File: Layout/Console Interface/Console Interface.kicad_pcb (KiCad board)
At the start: 2 copper layers, 25.5 x 5 mm, 54 parts, among them J1 USB_C_Receptacle_USB2.0, J2 Conn_01x04_Socket, J3 Conn_01x04_Socket, J4 Conn_01x04_Socket, J6 Conn_01x04_Socket, Q1 AO3401A, SW1 SW_BOOT, U1 W25Q32JVSS, U2 RP2040, U5 MIC5504-3.3YM5, Y1 Crystal_GND24

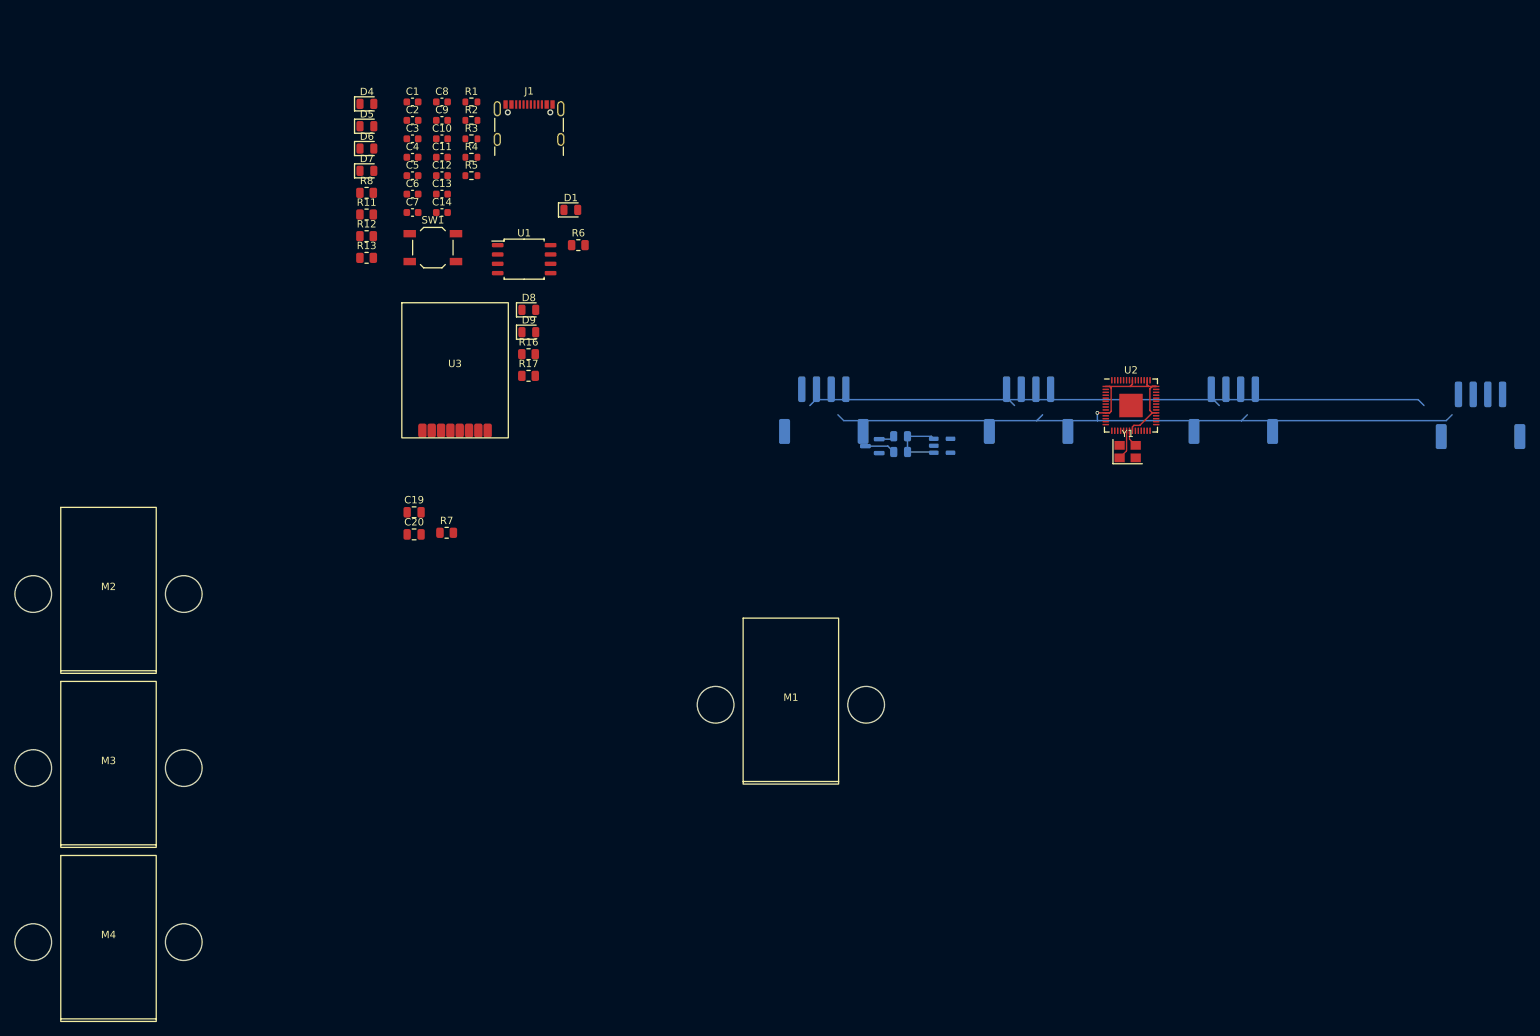
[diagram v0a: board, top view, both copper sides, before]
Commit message: Add console interface schematic
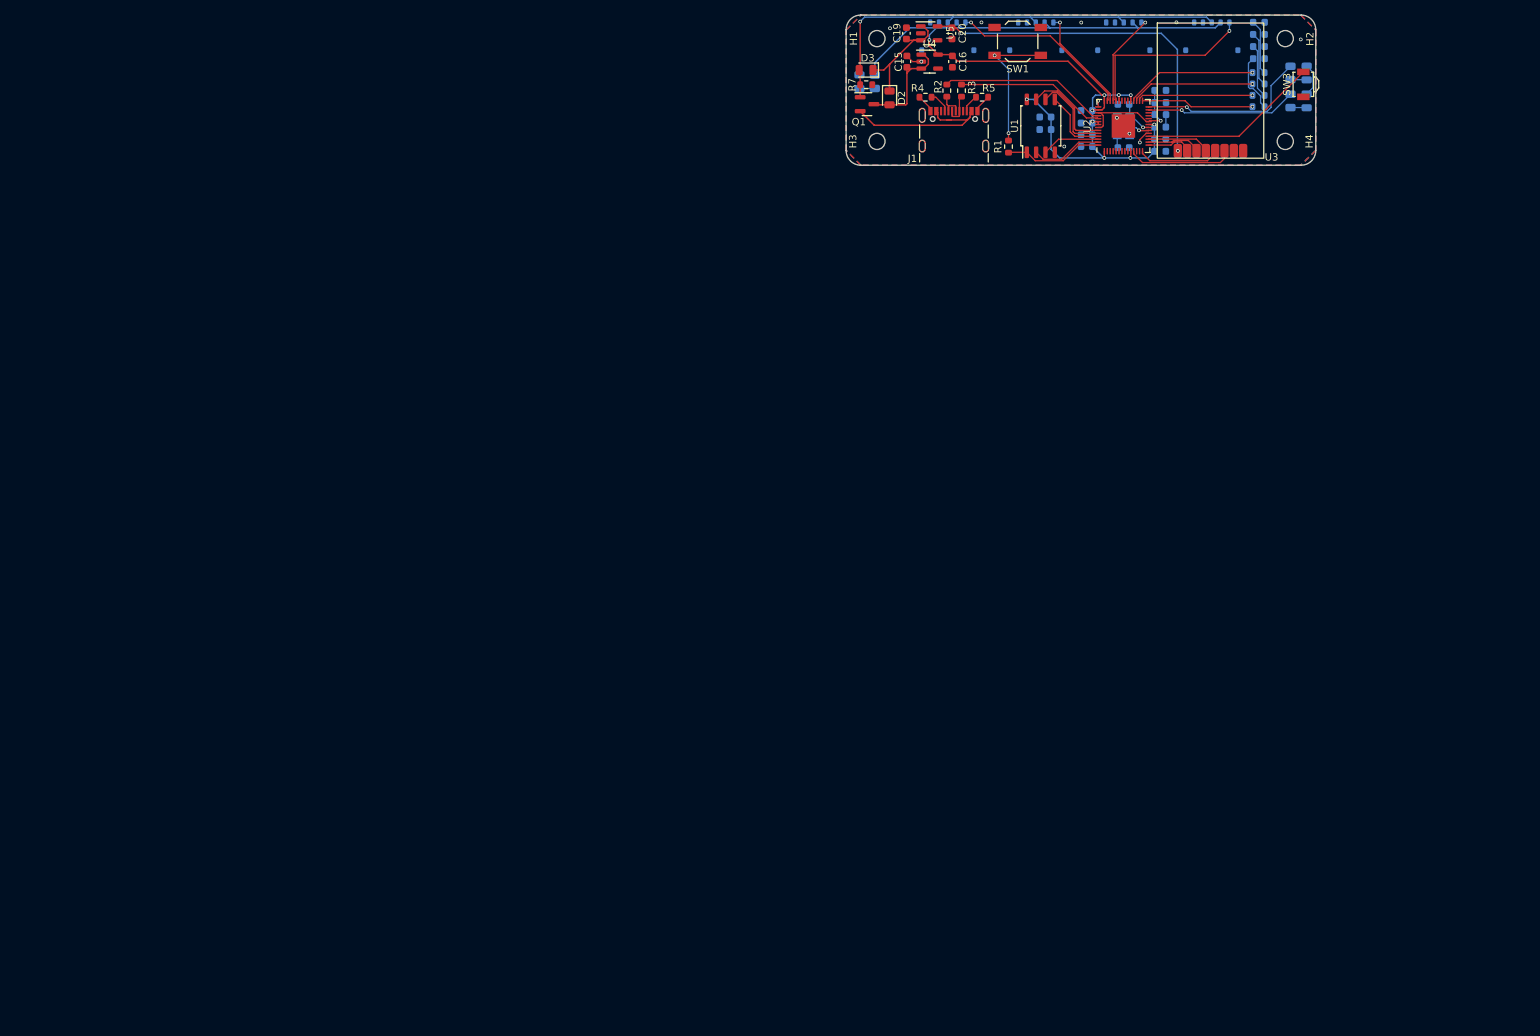
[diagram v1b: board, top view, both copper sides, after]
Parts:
- removed M1, M2, M3, M4: ~, GameCube Controllers:Controller Plug Clamp
- added C15: C, Capacitor_SMD:C_0603_1608Metric, F.Cu at (162.4, 39.6)
- added C16: C, Capacitor_SMD:C_0603_1608Metric, F.Cu at (168.6, 39.6)
- added H1: MountingHole, MountingHole:MountingHole_2.2mm_M2, F.Cu at (158.4, 36.5)
- added H2: MountingHole, MountingHole:MountingHole_2.2mm_M2, F.Cu at (214.0, 36.5)
- added H3: MountingHole, MountingHole:MountingHole_2.2mm_M2, F.Cu at (158.4, 50.5)
- added H4: MountingHole, MountingHole:MountingHole_2.2mm_M2, F.Cu at (214.0, 50.5)
- added SW3: SW_PAIR, Button_Switch_SMD:SW_SPST_B3U-3000P, F.Cu at (216.4, 42.7)
- added U4: MIC5504-3.3YM5, Package_TO_SOT_SMD:SOT-23-5, F.Cu at (165.5, 39.6)
- C1, C10, C11, C12, C13, C14, C2, C3, C4, C5, C6, C7, C8, C9, D1, D8, D9, R16, R17, R6, Y1: moved to B.Cu
- C19, C20: footprint Capacitor_SMD:C_0805_2012Metric -> Capacitor_SMD:C_0603_1608Metric
- D2, D3, Q1, U5: moved to F.Cu
- D4, D5, D6, D7: footprint LED_SMD:LED_0805_2012Metric -> LED_SMD:LED_0603_1608Metric; moved to B.Cu
- J2, J3, J4, J6: footprint Connector_JST:JST_PH_S4B-PH-SM4-TB_1x04-1MP_P2.00mm_Horizontal -> Connector_Molex:Molex_Pico-EZmate_78171-0005_1x05-1MP_P1.20mm_Vertical
- R11, R12, R13, R8: footprint Resistor_SMD:R_0805_2012Metric -> Resistor_SMD:R_0603_1608Metric; moved to B.Cu
- R7: footprint Resistor_SMD:R_0805_2012Metric -> Resistor_SMD:R_0603_1608Metric
- moved R13 123.2 mm to (210.3, 45.7)
- moved R12 123.0 mm to (210.3, 44.2)
- moved R11 122.8 mm to (210.3, 42.6)
- moved R8 122.6 mm to (210.3, 41.1)
- moved D7 122.4 mm to (210.4, 39.2), turned to 180 degrees
- moved D6 122.3 mm to (210.4, 37.5), turned to 180 degrees
- moved D5 122.1 mm to (210.4, 35.9), turned to 180 degrees
- moved D4 122.0 mm to (210.4, 34.2), turned to 180 degrees
- moved D8 110.7 mm to (216.9, 41.1), turned to -90 degrees
- moved R16 110.6 mm to (214.7, 41.1), turned to -90 degrees
- moved D9 110.5 mm to (216.9, 44.9), turned to -90 degrees
- moved R17 110.3 mm to (214.7, 44.9), turned to -90 degrees
- moved U3 109.7 mm to (203.8, 43.1)
- moved C7 103.2 mm to (197.0, 43.5)
- moved C6 102.6 mm to (197.0, 45.2)
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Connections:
- R6 pad 1: /Processor/PWR_LED -> +3.3V_A
- U2 pad 11: unconnected-(U2-GPIO8-Pad11) -> SPI0_MISO
- U2 pad 13: DATA_3 -> unconnected-(U2-GPIO10-Pad13)
- U2 pad 14: CONT_3 -> SPI0_MOSI
- U2 pad 15: SPI0_MISO -> NRF_CE
- U2 pad 18: SPI0_MOSI -> /Processor/PAIR
- U2 pad 2: CONT_1 -> unconnected-(U2-GPIO0-Pad2)
- U2 pad 27: NRF_CE -> RX_LED
- U2 pad 28: NRF_IRQ -> TX_LED
- U2 pad 3: DATA_1 -> unconnected-(U2-GPIO1-Pad3)
- U2 pad 30: DATA_4 -> CONT_3
- U2 pad 31: unconnected-(U2-GPIO20-Pad31) -> CONT_2
- U2 pad 32: unconnected-(U2-GPIO21-Pad32) -> CONT_1
- U2 pad 37: unconnected-(U2-GPIO25-Pad37) -> +3.3V_A
- U2 pad 38: PWR_ON -> DATA_4
- U2 pad 39: PWR_SW -> DATA_3
- U2 pad 4: /Processor/PAIR -> unconnected-(U2-GPIO2-Pad4)
- U2 pad 41: CONT_2 -> DATA_1
- U2 pad 48: +1V1 -> +3.3V_A
- U2 pad 5: /Processor/PWR_LED -> unconnected-(U2-GPIO3-Pad5)
- U2 pad 6: TX_LED -> unconnected-(U2-GPIO4-Pad6)
- U2 pad 7: RX_LED -> unconnected-(U2-GPIO5-Pad7)
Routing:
- net +3.3V: track 0.00 -> 47.8 mm, vias 0 -> 2
- net +5V: track 88.7 -> 61.9 mm, vias 0 -> 1
- net +3.3V_A: track 110.8 -> 135.5 mm, vias 1 -> 10
- net /Processor/PAIR: track 0.00 -> 24.7 mm
- net DATA_1: track 0.00 -> 24.4 mm, vias 0 -> 1
- net DATA_4: track 0.00 -> 24.3 mm, vias 0 -> 1
- net TX_LED: track 0.00 -> 23.9 mm, vias 0 -> 1
- net VBUS: track 0.31 -> 23.4 mm
- net /Processor/USB_DM: track 0.00 -> 22.8 mm
- net /Processor/USB_DP: track 0.00 -> 20.5 mm
- net RX_LED: track 0.00 -> 20.5 mm, vias 0 -> 1
- net Net-(R1-Pad2): track 0.00 -> 18.7 mm, vias 0 -> 2
- net CONT_1: track 0.00 -> 18.0 mm, vias 0 -> 1
- net CONT_2: track 0.00 -> 16.9 mm, vias 0 -> 1
- net +1V1: track 0.00 -> 16.6 mm, vias 0 -> 1
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- added copper zone on B.Cu, net GND
- added copper zone on F.Cu, net GND
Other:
- board size 25.5 x 5 mm -> 63.9 x 20.5 mm

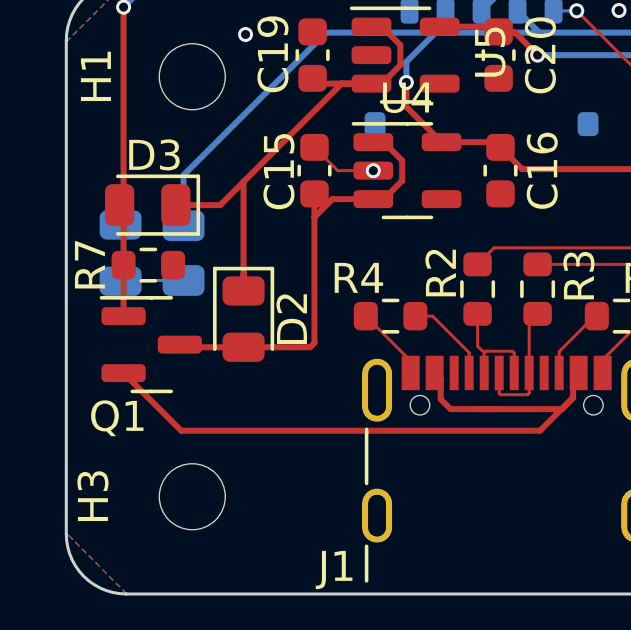
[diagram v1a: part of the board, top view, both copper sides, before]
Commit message: Fix missing ground
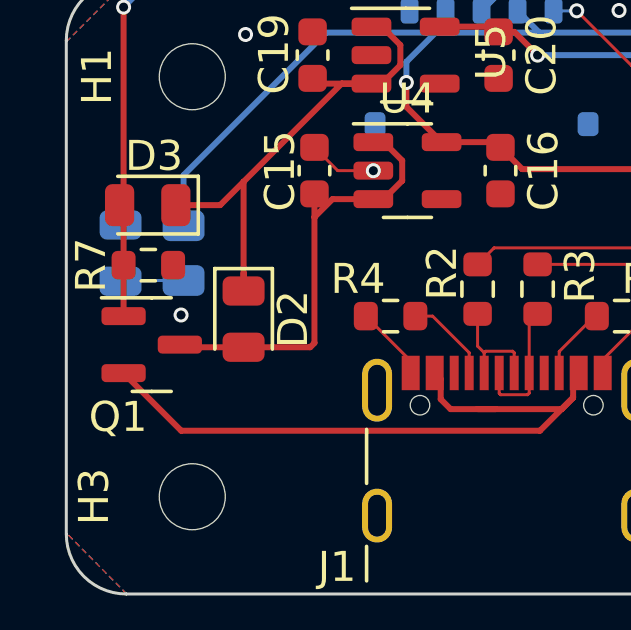
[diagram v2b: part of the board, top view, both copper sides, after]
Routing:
- net GND: vias 11 -> 12
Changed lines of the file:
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@@
   (via (at 188.5 44.91) (size 0.5) (drill 0.3) (layers "F.Cu" "B.Cu") (net 2))
   (via (at 192.76 49.4) (size 0.5) (drill 0.3) (layers "F.Cu" "B.Cu") (net 2))
+  (via (at 158 44.4) (size 0.5) (drill 0.3) (layers "F.Cu" "B.Cu") (free) (net 2))
   (via (at 216.08 36.57) (size 0.5) (drill 0.3) (layers "F.Cu" "B.Cu") (free) (net 2))
   (via (at 172.6 34.25) (size 0.5) (drill 0.3) (layers "F.Cu" "B.Cu") (free) (net 2))

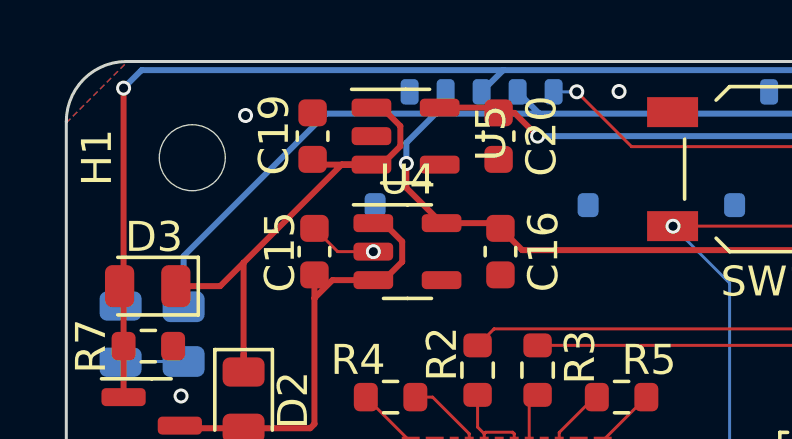
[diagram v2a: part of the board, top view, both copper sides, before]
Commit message: Fix another missing ground
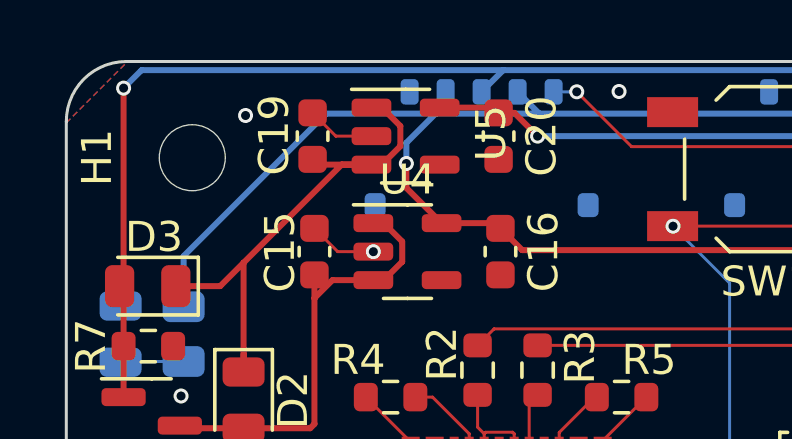
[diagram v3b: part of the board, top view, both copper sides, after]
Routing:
- net GND: track 16.3 -> 18.6 mm
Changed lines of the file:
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@@
   (segment (start 196.159685 48.50625) (end 196.159685 51.80625) (width 0.2) (layer "B.Cu") (net 1))
   (segment (start 165.654685 45.9325) (end 164.159685 44.4375) (width 0.1) (layer "F.Cu") (net 2))
+  (segment (start 163.159685 35.7375) (end 162.384685 34.9625) (width 0.1) (layer "F.Cu") (net 2))
   (segment (start 163.222185 39.5875) (end 162.447185 38.8125) (width 0.1) (layer "F.Cu") (net 2))
   (segment (start 194.17 50.220935) (end 194.17 50.6) (width 0.1) (layer "F.Cu") (net 2))
@@
   (segment (start 172.054685 46.3325) (end 172.054685 45.8925) (width 0.1) (layer "F.Cu") (net 2))
   (segment (start 164.41 39.59) (end 163.222185 39.5875) (width 0.1) (layer "F.Cu") (net 2))
+  (segment (start 164.347185 35.7375) (end 163.159685 35.7375) (width 0.1) (layer "F.Cu") (net 2))
   (segment (start 195.372185 49.35625) (end 195.034685 49.35625) (width 0.1) (layer "F.Cu") (net 2))
   (segment (start 165.654685 46.3325) (end 165.654685 45.9325) (width 0.1) (layer "F.Cu") (net 2))
